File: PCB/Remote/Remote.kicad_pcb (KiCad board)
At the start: 2 copper layers, 70 x 70 mm, 84 parts, among them J1 LCD, J2 DC, J3 TEMP, J4 LCD, J5 Reset, J6 USB-C-Socket-H, J7 TC2030-USB-NL-DS, T1 T3902_MEMS_Mic, U1 ESP32-S3-MINI-1, U2 SCD41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

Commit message: Library update
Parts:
- D4, D6: footprint RevK:SMD1010-Side -> RevK:SMD1010-Side2

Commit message: Library update
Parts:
- U7: footprint RevK:Sensirion_DFN-4_1.5x1.5mm_P0.5mm_SHT4x -> RevK:Sensirion_DFN-4_1.5x1.5mm_P0.5mm_SHT4x-Side

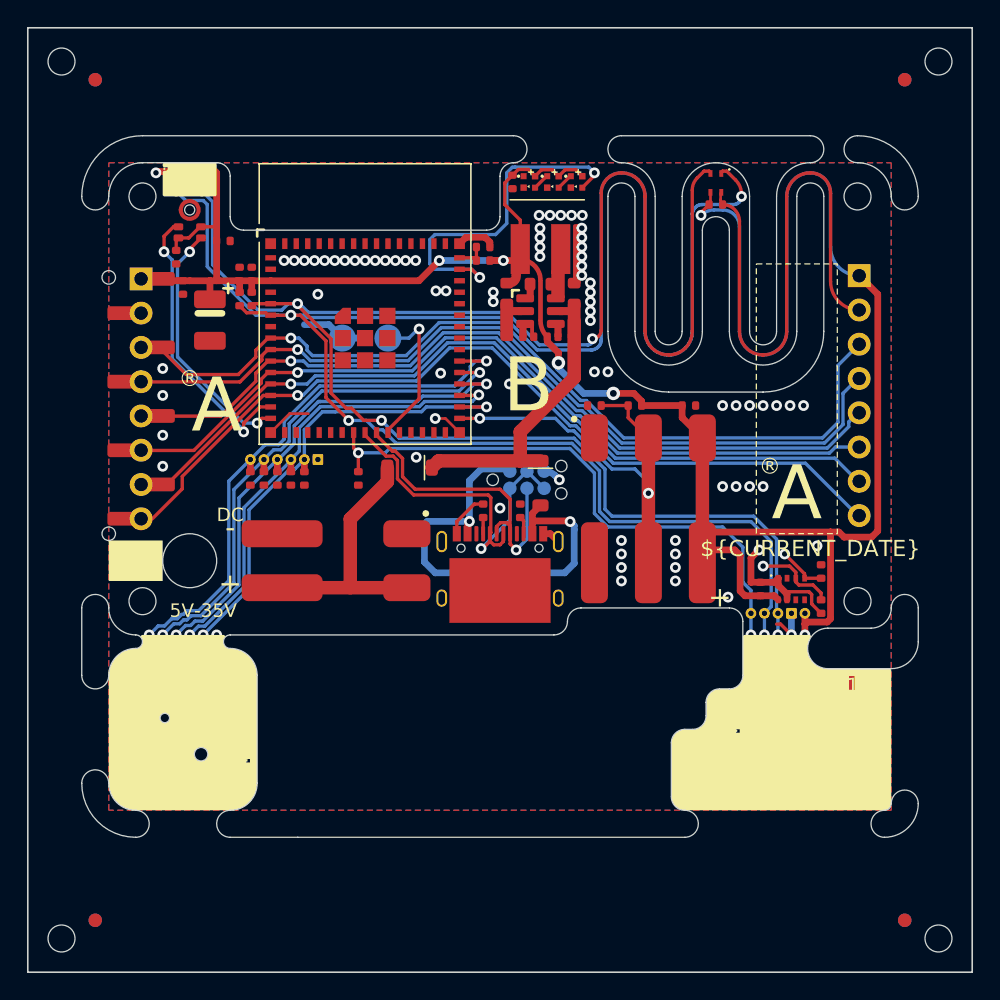
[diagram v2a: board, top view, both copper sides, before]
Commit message: New layout - IR back to sensible place
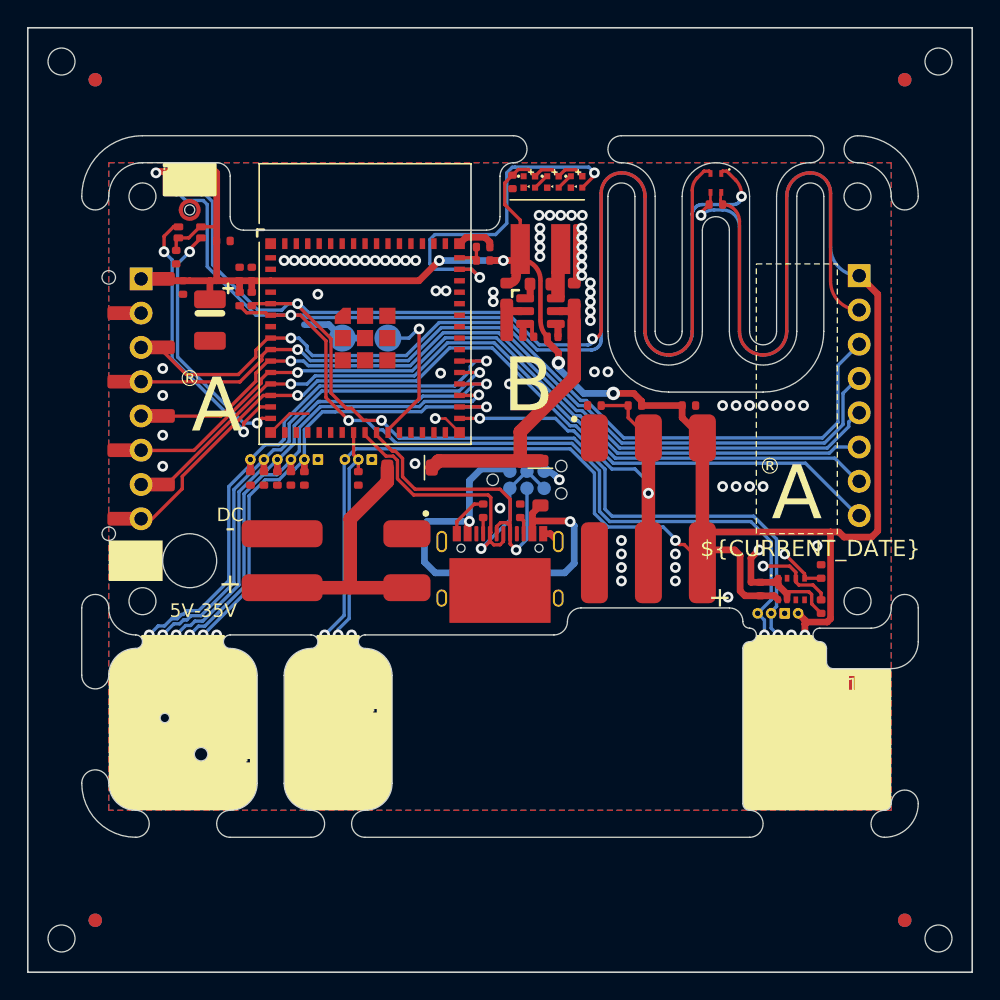
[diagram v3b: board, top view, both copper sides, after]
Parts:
- added TP22: TestPoint, RevK:TestPadSquare, F.Cu at (90.5, 97.0)
- added TP23: TestPoint, RevK:TestPad, F.Cu at (88.5, 97.0)
- added TP25: TestPoint, RevK:TestPadSquare, F.Cu at (89.0, 112.0)
- added TP26: TestPoint, RevK:TestPad, F.Cu at (87.0, 112.0)
- D5: footprint RevK:SMD1010-Side -> RevK:SMD1010-Side2
- moved TP21 31.3 mm to (89.5, 97.0)
- moved TP24 30.6 mm to (88.0, 112.0)
- moved R9 30.5 mm to (85.7, 113.5), turned to 45 degrees
- moved C13 29.8 mm to (88.0, 121.0), turned to 0 degrees
- moved U6 27.6 mm to (88.0, 117.5), turned to -90 degrees
- moved TP19 0.54 mm to (122.1, 112.0)
- moved TP17 0.52 mm to (119.1, 112.0)
- moved TP18 0.52 mm to (120.1, 112.0)
- moved TP20 0.52 mm to (121.1, 112.0)
- moved TP13 0.50 mm to (119.1, 108.4)
- moved TP14 0.50 mm to (120.1, 108.4)
- moved TP15 0.50 mm to (122.1, 108.4)
- moved TP16 0.50 mm to (121.1, 108.4)
- moved C5 0.10 mm to (121.7, 111.0)
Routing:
- net IR: track 53.6 -> 24.0 mm, vias 2 -> 1
- net +3.3V: track 223.8 -> 250.1 mm, vias 8 -> 9
- net GND: track 102.2 -> 91.2 mm, vias 84 -> 90
- net Net-(U6-VCC): track 5.62 -> 8.58 mm
- net SDA: track 163.7 -> 164.9 mm
- net P: track 47.8 -> 48.9 mm
- net N: track 46.2 -> 47.1 mm
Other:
- board text removed: "2.4{dblquote}LCD"

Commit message: SS
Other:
- board text added: "+ -"
- board text added: "+ 2{dblquote}LCD DIN CLK CS DC RST BL"
- board text added: "Faikin Remote / Env Monitor"
- board text removed: "2{dblquote}LCD"
- board text removed: "BL"
- board text removed: "DIN CLK CS DC RST"
- board text removed: "Faikin Remote"

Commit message: SS
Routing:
- net GND: track 91.2 -> 96.2 mm, vias 90 -> 96
- net +3.3V: track 250.1 -> 248.0 mm
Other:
- board text added: "remote.revk.uk"

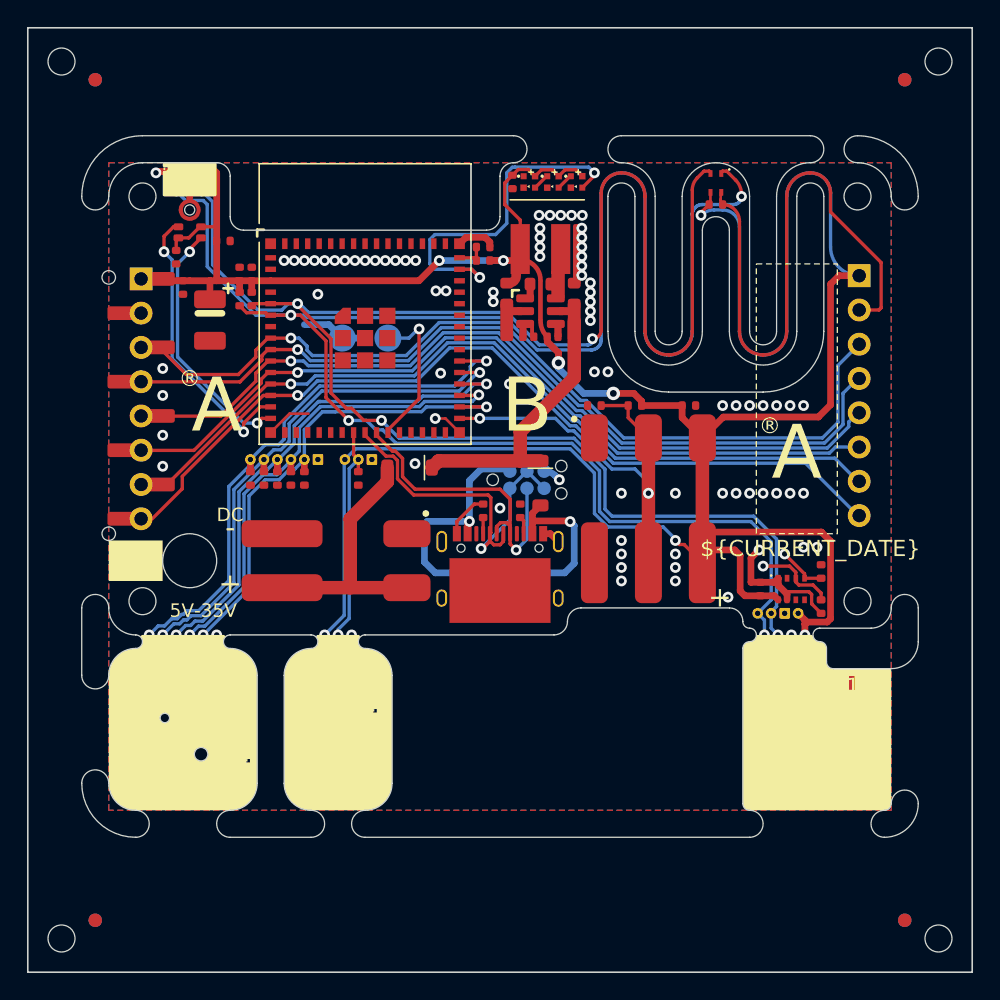
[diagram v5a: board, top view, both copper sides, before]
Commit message: Moved mic
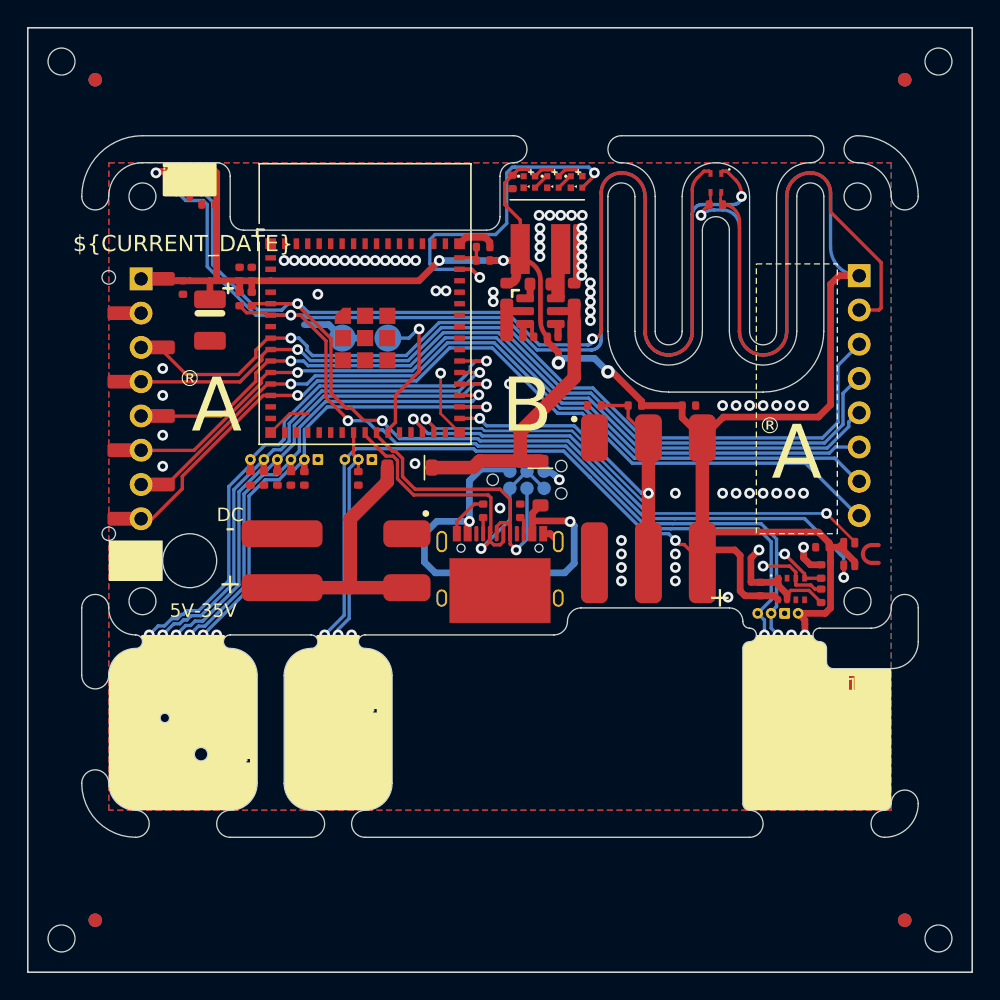
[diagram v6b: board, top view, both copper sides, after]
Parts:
- T1: footprint RevK:T3902_MEMS_Mic -> RevK:T3902_MEMS_Mic-Open
- moved T1 55.6 mm to (126.8, 104.0), turned to 90 degrees
- moved C12 52.5 mm to (123.9, 103.5), turned to 180 degrees
- moved C9 2.92 mm to (78.4, 78.1), turned to 180 degrees
- moved D14 0.80 mm to (123.8, 107.1)
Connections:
- U1 pad 14: MCLK -> unconnected-(U1-GPIO10-Pad14)
- U1 pad 15: MDATA -> unconnected-(U1-GPIO11-Pad15)
- U1 pad 28: unconnected-(U1-GPIO33-Pad28) -> MDATA
- U1 pad 29: unconnected-(U1-GPIO34-Pad29) -> MCLK
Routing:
- net MDATA: track 18.6 -> 39.8 mm
- net MCLK: track 21.4 -> 36.9 mm
- net GND: track 96.2 -> 99.8 mm, vias 96 -> 91
- net +3.3V: track 248.0 -> 245.3 mm
- net SDA: track 164.9 -> 162.7 mm
- net SCL: track 154.0 -> 152.2 mm
- net P: track 48.9 -> 48.1 mm
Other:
- board text added: "33"
- board text added: "34"
- board text added: "LCD"
- board text removed: "10"
- board text removed: "11"

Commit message: Library update
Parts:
- T1: footprint RevK:T3902_MEMS_Mic-Open -> RevK:T3902_MEMS_Mic_Open

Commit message: SS
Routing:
- net GND: track 99.8 -> 103.7 mm
- net +3.3V: track 245.3 -> 246.6 mm
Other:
- board text added: "Env monitor"
- board text added: "Faikin Remote"
- board text added: "U"
- board text removed: "Faikin Remote / Env Monitor"
